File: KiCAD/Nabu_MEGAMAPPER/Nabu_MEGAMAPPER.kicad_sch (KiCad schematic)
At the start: 15 parts, among them J1 Z80 Socket Header, J2 Z80 Socket Header, U1 Z80CPU, U10 74LS374, U11 74LS374, U12 74LS85, U13 XC9536PC44, U2 AS6C4008-55PCN, U3 74LS670, U4 74LS670, U5 HM6116, U6 74LS157, U7 74LS157, U8 74LS157, U9 74LS244

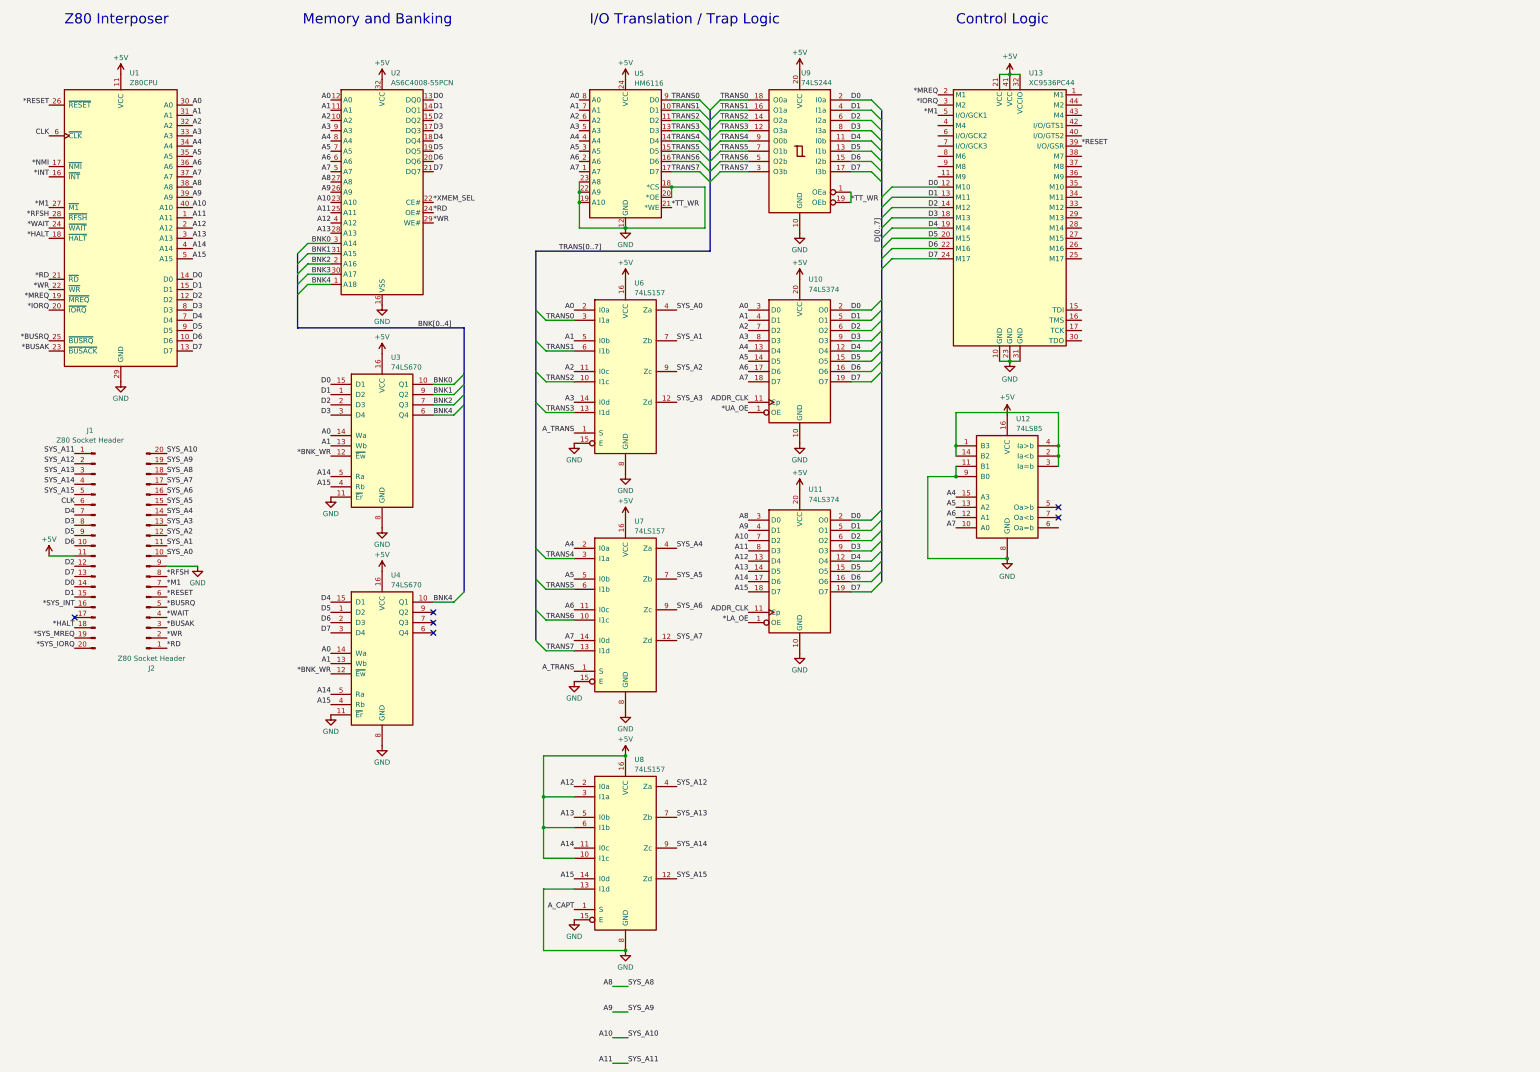
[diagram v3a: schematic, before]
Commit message: Started laying out MegaMapper PCB
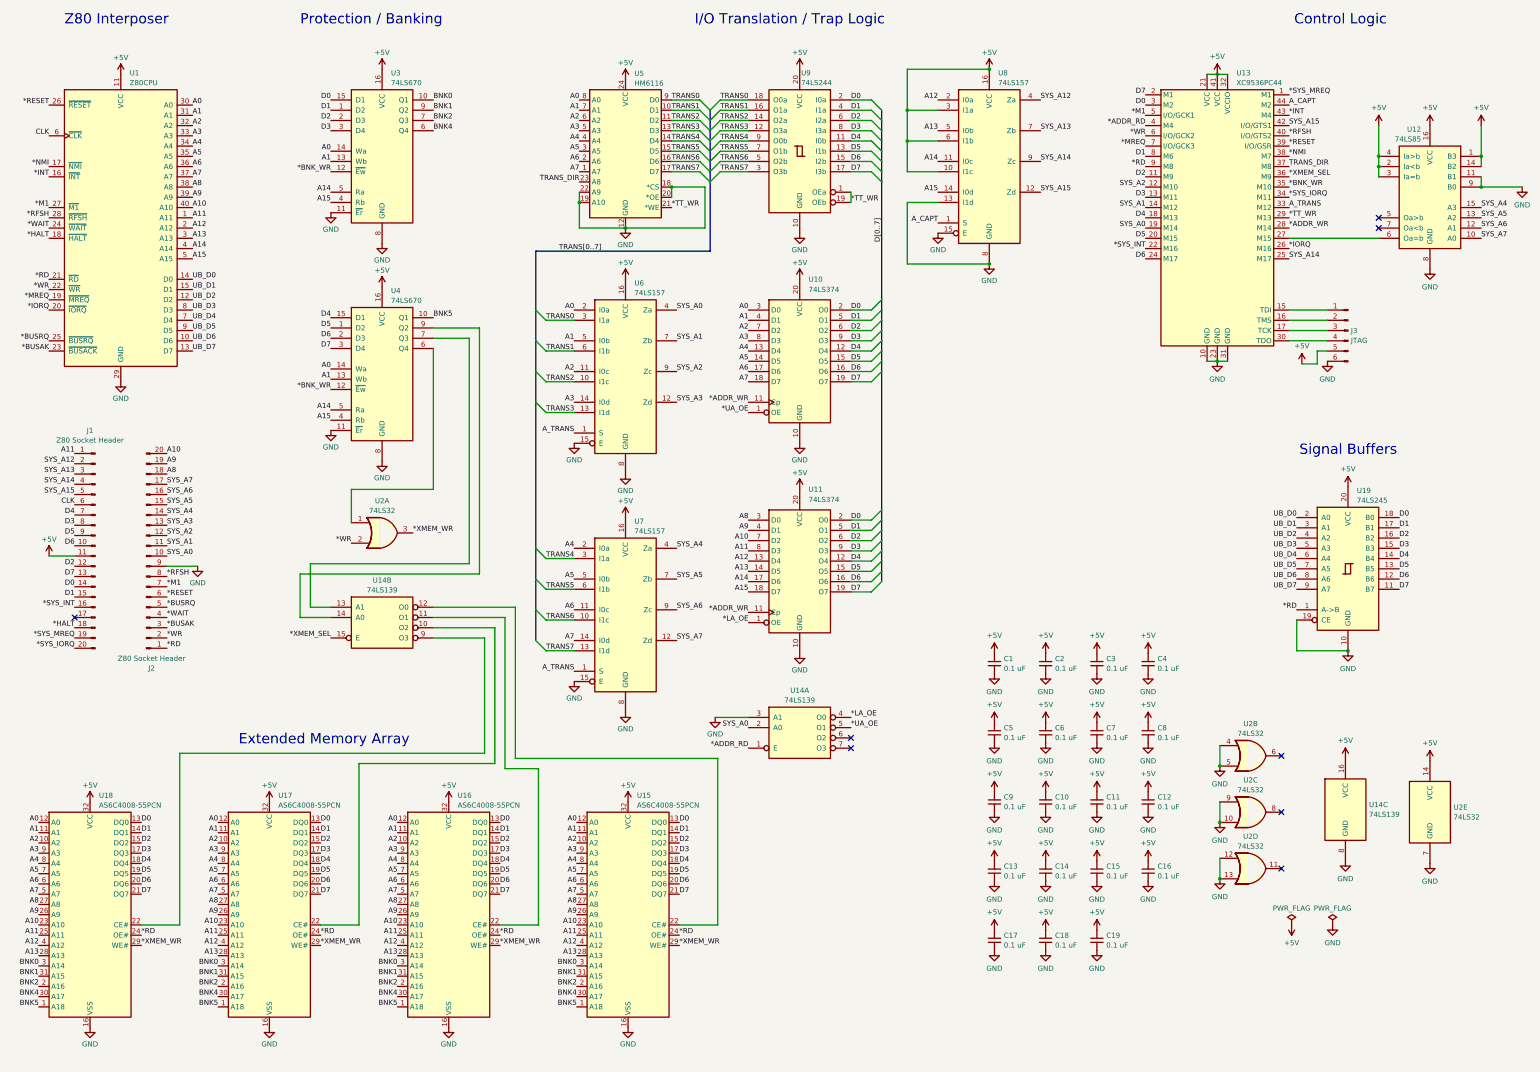
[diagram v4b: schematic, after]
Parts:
- added C1, C10, C11, C12, C13, C14, C15, C16, C17, C18, C19, C2, C3, C4, C5, C6, C7, C8, C9: 0.1 uF, Capacitor_THT:C_Disc_D5.0mm_W2.5mm_P5.00mm, symbol Device:C_Small
- added J3: JTAG, Connector_PinHeader_2.54mm:PinHeader_1x06_P2.54mm_Vertical, symbol Connector:Conn_01x06_Pin
- added U14: 74LS139, Package_DIP:DIP-16_W7.62mm, symbol 74xx:74LS139
- added U15, U16, U17: AS6C4008-55PCN, Package_DIP:DIP-32_W15.24mm, symbol Memory_RAM:AS6C4008-55PCN
- added U19: 74LS245, Package_DIP:DIP-20_W7.62mm, symbol 74xx:74LS245
- added U2: 74LS32, Package_DIP:DIP-14_W7.62mm, symbol 74xx:74LS32
- J1, J2: footprint (none) -> Connector_PinHeader_2.54mm:PinHeader_1x20_P2.54mm_Vertical
- U1: footprint (none) -> Package_DIP:DIP-40_W15.24mm
- U10, U11, U9: footprint (none) -> Package_DIP:DIP-20_W7.62mm
- U12, U3, U4, U6, U7, U8: footprint (none) -> Package_DIP:DIP-16_W7.62mm
- U13: footprint (none) -> Package_LCC:PLCC-44_THT-Socket
- U5: footprint (none) -> Package_DIP:DIP-24_W15.24mm
- renumbered U2 to U18
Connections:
- net ADDR_CLK is gone; now on net *ADDR_WR: U10.11 (Cp), U11.11 (Cp)
- net BNK3 is gone; now on net BNK4: U18.30 (A17)
- net *BNK_WR: now also U13.35 (M10)
- net *INT: now also U13.43 (M4)
- net *IORQ: now also U13.26 (M16); no longer U13.3 (M2)
- net *LA_OE: now also U14.4 (O0)
- net *MREQ: now also U13.7 (I/O/GCK3); no longer U13.2 (M1)
- net *NMI: now also U13.38 (M7)
- net *RD: now also U13.9 (M8), U15.24 (OE#), U16.24 (OE#), U17.24 (OE#), U19.1 (A->B)
- net *RFSH: now also U13.40 (I/O/GTS2)
- net *SYS_INT: now also U13.22 (M16)
- net *SYS_IORQ: now also U13.34 (M11)
- net *SYS_MREQ: now also U13.1 (M1)
- net *TT_WR: now also U13.29 (M13)
- net *UA_OE: now also U14.5 (O1)
- net *WR: now also U13.6 (I/O/GCK2), U2.2; no longer U18.29 (WE#)
- net *XMEM_SEL: now also U13.36 (M9), U14.15 (E); no longer U18.22 (CE#)
- net +5V: now also U12.1 (B3), U12.14 (B2), U12.2 (Ia<b), U12.3 (Ia=b), U12.4 (Ia>b), C1.1, C10.1, C11.1, C12.1, C13.1, C14.1, C15.1, C16.1, C17.1, C18.1, C19.1, C2.1, C3.1, C4.1, C5.1, C6.1, C7.1, C8.1, C9.1, J3.5 (Pin_5), U14.16 (VCC), U15.32 (VCC), U16.32 (VCC), U17.32 (VCC), U19.20 (VCC), U2.14 (VCC)
- net A0: now also U15.12 (A0), U16.12 (A0), U17.12 (A0)
- net A1: now also U15.11 (A1), U16.11 (A1), U17.11 (A1)
- net A10: now also U15.23 (A10), U16.23 (A10), U17.23 (A10)
- net A11: now also U15.25 (A11), U16.25 (A11), U17.25 (A11)
- net A12: now also U15.4 (A12), U16.4 (A12), U17.4 (A12)
- net A13: now also U15.28 (A13), U16.28 (A13), U17.28 (A13)
- net A2: now also U15.10 (A2), U16.10 (A2), U17.10 (A2)
- net A3: now also U15.9 (A3), U16.9 (A3), U17.9 (A3)
- net A4: now also U15.8 (A4), U16.8 (A4), U17.8 (A4); no longer U12.15 (A3)
- net A5: now also U15.7 (A5), U16.7 (A5), U17.7 (A5); no longer U12.13 (A2)
- net A6: now also U15.6 (A6), U16.6 (A6), U17.6 (A6); no longer U12.12 (A1)
- net A7: now also U15.5 (A7), U16.5 (A7), U17.5 (A7); no longer U12.10 (A0)
- net A8: now also U15.27 (A8), U16.27 (A8), U17.27 (A8)
- net A9: now also U15.26 (A9), U16.26 (A9), U17.26 (A9)
- net A_CAPT: now also U13.44 (M2)
- net A_TRANS: now also U13.33 (M12)
- net BNK0: now also U15.3 (A14), U16.3 (A14), U17.3 (A14)
- net BNK1: now also U15.31 (A15), U16.31 (A15), U17.31 (A15)
- net BNK2: now also U15.2 (A16), U16.2 (A16), U17.2 (A16)
- net BNK4: now also U15.30 (A17), U16.30 (A17), U17.30 (A17); no longer U18.1 (A18), U4.10 (Q1)
- net D0: now also U13.3 (M2), U15.13 (DQ0), U16.13 (DQ0), U17.13 (DQ0), U19.18 (B0); no longer U1.14 (D0), U13.12 (M10)
- net D1: now also U13.8 (M6), U15.14 (DQ1), U16.14 (DQ1), U17.14 (DQ1), U19.17 (B1); no longer U1.15 (D1), U13.13 (M11)
- net D2: now also U13.11 (M9), U15.15 (DQ2), U16.15 (DQ2), U17.15 (DQ2), U19.16 (B2); no longer U1.12 (D2), U13.14 (M12)
- net D3: now also U13.13 (M11), U15.17 (DQ3), U16.17 (DQ3), U17.17 (DQ3), U19.15 (B3); no longer U1.8 (D3), U13.18 (M13)
- net D4: now also U13.18 (M13), U15.18 (DQ4), U16.18 (DQ4), U17.18 (DQ4), U19.14 (B4); no longer U1.7 (D4), U13.19 (M14)
- net D5: now also U15.19 (DQ5), U16.19 (DQ5), U17.19 (DQ5), U19.13 (B5); no longer U1.9 (D5)
- net D6: now also U13.24 (M17), U15.20 (DQ6), U16.20 (DQ6), U17.20 (DQ6), U19.12 (B6); no longer U1.10 (D6), U13.22 (M16)
- net D7: now also U13.2 (M1), U15.21 (DQ7), U16.21 (DQ7), U17.21 (DQ7), U19.11 (B7); no longer U1.13 (D7), U13.24 (M17)
- net GND: now also C1.2, C10.2, C11.2, C12.2, C13.2, C14.2, C15.2, C16.2, C17.2, C18.2, C19.2, C2.2, C3.2, C4.2, C5.2, C6.2, C7.2, C8.2, C9.2, J3.6 (Pin_6), U14.3 (A1), U14.8 (GND), U15.16 (VSS), U16.16 (VSS), U17.16 (VSS), U19.10 (GND), U19.19 (CE), U2.10, U2.12, U2.13, U2.4, U2.5, U2.7 (GND), U2.9; no longer U5.23 (A8)
- net SYS_A0: now also U13.19 (M14), U14.2 (A0)
- net SYS_A1: now also U13.14 (M12)
- net SYS_A14: now also U13.25 (M17)
- net SYS_A15: now also U13.42 (I/O/GTS1)
- net SYS_A2: now also U13.12 (M10)
- net SYS_A4: now also U12.15 (A3)
- net SYS_A5: now also U12.13 (A2)
- net SYS_A6: now also U12.12 (A1)
- net SYS_A7: now also U12.10 (A0)
- net at U4.6 (Q4): now also U2.1
- net at U4.7 (Q3): now also U14.13 (A1)
- net at U4.9 (Q2): now also U14.14 (A0)
- net at U13.15 (TDI): now also J3.1 (Pin_1)
- net at U13.16 (TMS): now also J3.2 (Pin_2)
- net at U13.17 (TCK): now also J3.3 (Pin_3)
- net at U13.27 (M15): now also U12.6 (Oa=b)
- net *ADDR_WR: now reaches U13.28 (M14)
- net at U13.30 (TDO): now also J3.4 (Pin_4)
- net TRANS_DIR: now reaches U13.37 (M8)
- net TRANS_DIR: now also U5.23 (A8)
- net *ADDR_RD: now reaches U13.4 (M4)
- net *ADDR_RD: now also U14.1 (E)
- new net: U14.10 (O2), U17.22 (CE#)
- new net: U14.11 (O1), U16.22 (CE#)
- new net: U14.12 (O0), U15.22 (CE#)
- new net: U14.9 (O3), U18.22 (CE#)
- new net *XMEM_WR: U15.29 (WE#), U16.29 (WE#), U17.29 (WE#), U18.29 (WE#), U2.3
- new net BNK5: U15.1 (A18), U16.1 (A18), U17.1 (A18), U18.1 (A18), U4.10 (Q1)
- new net UB_D0: U1.14 (D0), U19.2 (A0)
- new net UB_D1: U1.15 (D1), U19.3 (A1)
- new net UB_D2: U1.12 (D2), U19.4 (A2)
- new net UB_D3: U1.8 (D3), U19.5 (A3)
- new net UB_D4: U1.7 (D4), U19.6 (A4)
- new net UB_D5: U1.9 (D5), U19.7 (A5)
- new net UB_D6: U1.10 (D6), U19.8 (A6)
- new net UB_D7: U1.13 (D7), U19.9 (A7)
- no-connect marks 6 -> 8
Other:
- note added: "Extended Memory Array"
- note added: "Protection / Banking"
- note added: "Signal Buffers"
- note removed: "Memory and Banking"
- title: (none) -> Z80 MEGAMAPPER (NABU Ver.)
- moved on the sheet: U12, U13, U18, U3, U4, U8

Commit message: Continued work on PCB layout
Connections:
- net *RD: now also U2.4, U2.5; no longer J2.1 (Pin_1)
- net A14: now also U13.25 (M17)
- net A15: now also U13.42 (I/O/GTS1)
- net GND: no longer U2.4, U2.5
- net SYS_A14: no longer U13.25 (M17)
- net SYS_A15: no longer U13.42 (I/O/GTS1)
- net at U2.6: now also J2.1 (Pin_1)
- net *XMEM_WR: no longer names the net of U15.29 (WE#), U16.29 (WE#), U17.29 (WE#), U18.29 (WE#), U2.3
- no-connect marks 8 -> 7
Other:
- moved on the sheet: U19, U2A, U2B

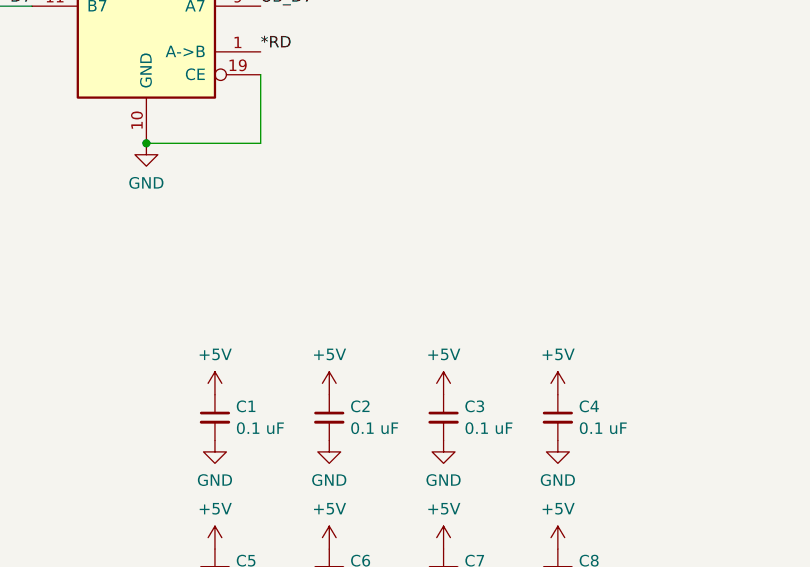
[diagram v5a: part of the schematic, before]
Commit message: Added bulk storage capacitor and started designing layout
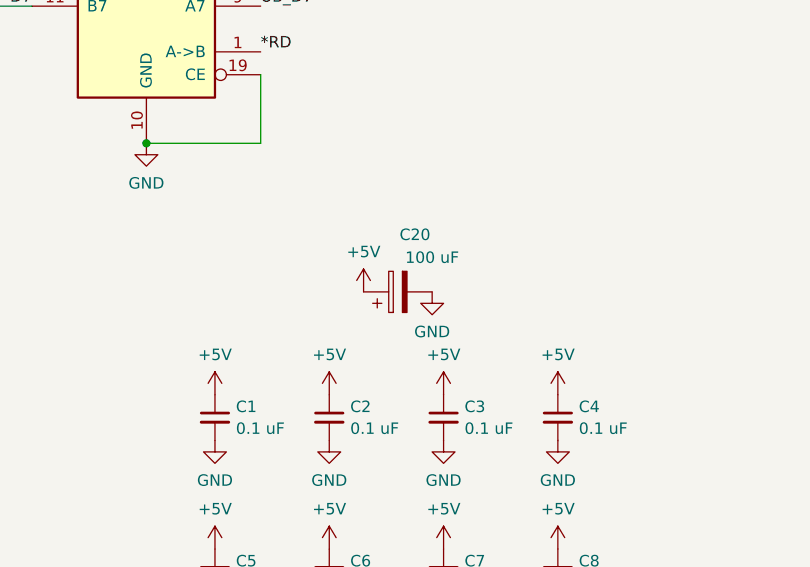
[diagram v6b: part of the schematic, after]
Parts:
- added C20: 100 uF, Capacitor_THT:CP_Radial_D6.3mm_P2.50mm, symbol Device:C_Polarized
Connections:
- net +5V: now also C20.1
- net GND: now also C20.2
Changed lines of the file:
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@@
+    )
+  )
+  (symbol (lib_id "Device:C_Polarized") (at 281.305 164.465 90) (unit 1)
+    (in_bom yes) (on_board yes) (dnp no)
+    (property "Reference" "C20" (at 283.21 158.115 90)
+      (effects (font (size 1.27 1.27)))
+    )
+    (property "Value" "100 uF" (at 285.115 160.655 90)
+      (effects (font (size 1.27 1.27)))
+    )
+    (property "Footprint" "Capacitor_THT:CP_Radial_D6.3mm_P2.50mm" (at 285.115 163.4998 0)
+      (effects (font (size 1.27 1.27)) hide)
+    )
+    (property "Datasheet" "~" (at 281.305 164.465 0)
+      (effects (font (size 1.27 1.27)) hide)
+    )
+    (pin "1")
+    (pin "2")
+    (instances
+      (project "Nabu_MEGAMAPPER"
+        (path "/08a88c4b-5d36-43ed-bafe-b5ff1ee4c2dd"
+          (reference "C20") (unit 1)
+        )
+      )
     )
   )
@@
     )
   )
+  (symbol (lib_id "power:GND") (at 285.115 164.465 0) (mirror y) (unit 1)
+    (in_bom yes) (on_board yes) (dnp no) (fields_autoplaced)
+    (property "Reference" "#PWR095" (at 285.115 170.815 0)
+      (effects (font (size 1.27 1.27)) hide)
+    )
+    (property "Value" "GND" (at 285.115 168.91 0)
+      (effects (font (size 1.27 1.27)))
+    )
+    (property "Footprint" "" (at 285.115 164.465 0)
+      (effects (font (size 1.27 1.27)) hide)
+    )
+    (property "Datasheet" "" (at 285.115 164.465 0)
+      (effects (font (size 1.27 1.27)) hide)
+    )
+    (pin "1")
+    (instances
+      (project "Nabu_MEGAMAPPER"
+        (path "/08a88c4b-5d36-43ed-bafe-b5ff1ee4c2dd"
+          (reference "#PWR095") (unit 1)
+        )
+      )
+    )
+  )
   (symbol (lib_id "power:GND") (at 156.845 182.88 0) (unit 1)
     (in_bom yes) (on_board yes) (dnp no) (fields_autoplaced)
@@
         )
       )
+    )
+  )
+  (symbol (lib_id "power:+5V") (at 277.495 164.465 0) (mirror y) (unit 1)
+    (in_bom yes) (on_board yes) (dnp no) (fields_autoplaced)
+    (property "Reference" "#PWR048" (at 277.495 168.275 0)
+      (effects (font (size 1.27 1.27)) hide)
+    )
+    (property "Value" "+5V" (at 277.495 160.02 0)
+      (effects (font (size 1.27 1.27)))
+    )
+    (property "Footprint" "" (at 277.495 164.465 0)
+      (effects (font (size 1.27 1.27)) hide)
+    )
+    (property "Datasheet" "" (at 277.495 164.465 0)
+      (effects (font (size 1.27 1.27)) hide)
+    )
+    (pin "1")
+    (instances
+      (project "Nabu_MEGAMAPPER"
+        (path "/08a88c4b-5d36-43ed-bafe-b5ff1ee4c2dd"
+          (reference "#PWR048") (unit 1)
+        )
+      )
